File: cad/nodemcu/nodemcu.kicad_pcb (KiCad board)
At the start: 2 copper layers, 1 part, among them P1 CONN_02X15

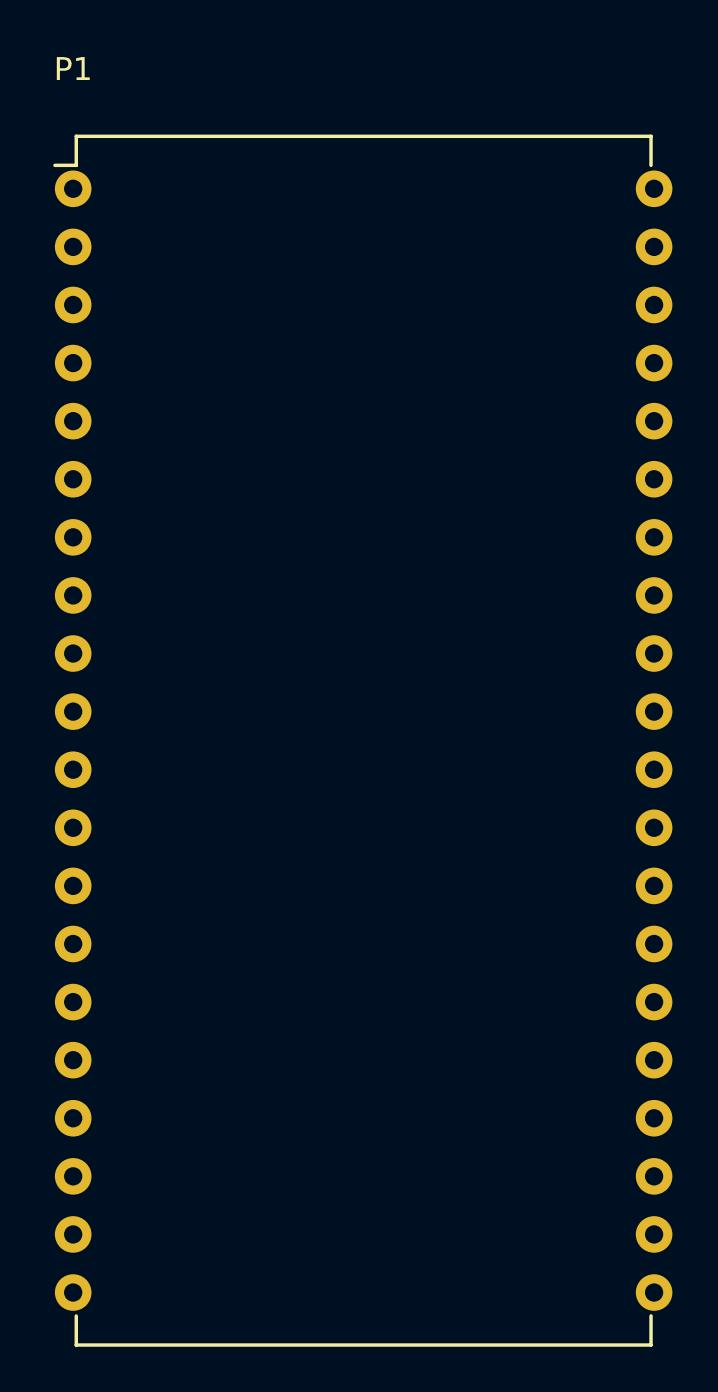
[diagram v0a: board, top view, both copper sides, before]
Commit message: added schematic for nodemcu
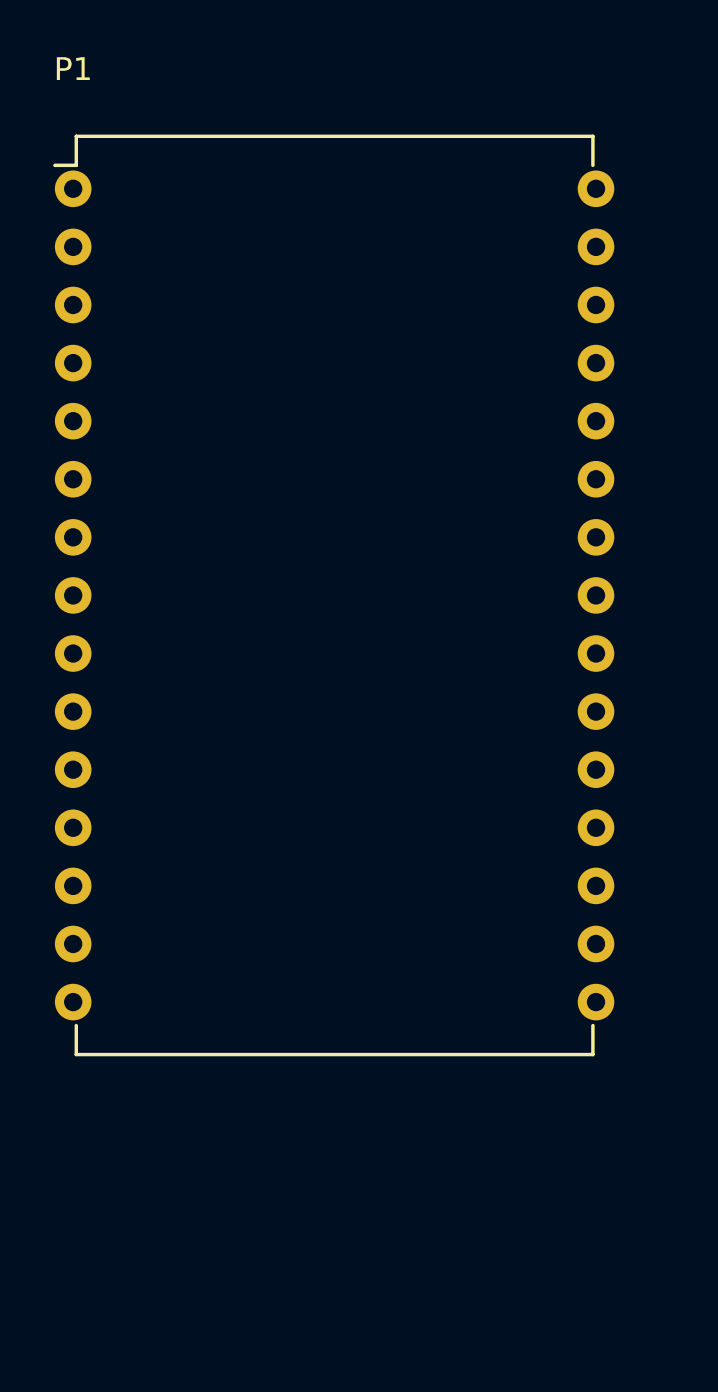
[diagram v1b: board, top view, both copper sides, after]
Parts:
- P1: value CONN_02X15 -> NodeMCU; footprint Housings_DIP:DIP-40_W25.4mm -> nodemcu:NodeMCU
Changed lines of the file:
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@@
     (links 0)
     (no_connects 0)
-    (area 143.392767 98.6586 175.176101 155.978601)
+    (area 144.773719 98.6586 172.626101 143.329253)
     (thickness 1.6)
     (drawings 0)
@@
     (add_net "Net-(P1-Pad9)")
   )
-  (module Housings_DIP:DIP-40_W25.4mm (layer F.Cu)
+  (module nodemcu:NodeMCU (layer F.Cu)
     (at 148.5011 105.0036)
-    (descr "40-lead dip package, row spacing 25.4 mm (1000 mils)")
-    (tags "dil dip 2.54 1000")
+    (descr "64-lead dip package, row spacing 22.86 mm (900 mils)")
+    (tags "dil dip 2.54 900")
     (fp_text reference P1 (at 0 -5.22) (layer F.SilkS)
       (effects (font (size 1 1) (thickness 0.15)))
     )
-    (fp_text value CONN_02X15 (at 0 -3.72) (layer F.Fab)
+    (fp_text value NodeMCU (at 0 -3.72) (layer F.Fab)
       (effects (font (size 1 1) (thickness 0.15)))
     )
-    (fp_line (start -1.05 -2.45) (end -1.05 50.75) (layer F.CrtYd) (width 0.05))
-    (fp_line (start 26.45 -2.45) (end 26.45 50.75) (layer F.CrtYd) (width 0.05))
-    (fp_line (start -1.05 -2.45) (end 26.45 -2.45) (layer F.CrtYd) (width 0.05))
-    (fp_line (start -1.05 50.75) (end 26.45 50.75) (layer F.CrtYd) (width 0.05))
+    (fp_line (start -1.05 -2.45) (end -1.05 38.100596) (layer F.CrtYd) (width 0.05))
+    (fp_line (start 23.9 -2.45) (end 23.9 38.100652) (layer F.CrtYd) (width 0.05))
+    (fp_line (start -1.05 -2.45) (end 23.9 -2.45) (layer F.CrtYd) (width 0.05))
+    (fp_line (start -1.05 38.02) (end 23.9 38.02) (layer F.CrtYd) (width 0.05))
     (fp_line (start 0.135 -2.295) (end 0.135 -1.025) (layer F.SilkS) (width 0.15))
-    (fp_line (start 25.265 -2.295) (end 25.265 -1.025) (layer F.SilkS) (width 0.15))
-    (fp_line (start 25.265 50.555) (end 25.265 49.285) (layer F.SilkS) (width 0.15))
-    (fp_line (start 0.135 50.555) (end 0.135 49.285) (layer F.SilkS) (width 0.15))
-    (fp_line (start 0.135 -2.295) (end 25.265 -2.295) (layer F.SilkS) (width 0.15))
-    (fp_line (start 0.135 50.555) (end 25.265 50.555) (layer F.SilkS) (width 0.15))
+    (fp_line (start 22.725 -2.295) (end 22.725 -1.025) (layer F.SilkS) (width 0.15))
+    (fp_line (start 22.725 37.855) (end 22.725 36.585) (layer F.SilkS) (width 0.15))
+    (fp_line (start 0.135 37.855) (end 0.135 36.585) (layer F.SilkS) (width 0.15))
+    (fp_line (start 0.135 -2.295) (end 22.725 -2.295) (layer F.SilkS) (width 0.15))
+    (fp_line (start 0.135 37.855) (end 22.725 37.855) (layer F.SilkS) (width 0.15))
     (fp_line (start 0.135 -1.025) (end -0.8 -1.025) (layer F.SilkS) (width 0.15))
     (pad 1 thru_hole oval (at 0 0) (size 1.6 1.6) (drill 0.8) (layers *.Cu *.Mask F.SilkS)
@@
     (pad 15 thru_hole oval (at 0 35.56) (size 1.6 1.6) (drill 0.8) (layers *.Cu *.Mask F.SilkS)
       (net 15 "Net-(P1-Pad15)"))
-    (pad 16 thru_hole oval (at 0 38.1) (size 1.6 1.6) (drill 0.8) (layers *.Cu *.Mask F.SilkS)
+    (pad 16 thru_hole oval (at 22.86 35.56) (size 1.6 1.6) (drill 0.8) (layers *.Cu *.Mask F.SilkS)
       (net 16 "Net-(P1-Pad16)"))
-    (pad 17 thru_hole oval (at 0 40.64) (size 1.6 1.6) (drill 0.8) (layers *.Cu *.Mask F.SilkS)
+    (pad 17 thru_hole oval (at 22.86 33.02) (size 1.6 1.6) (drill 0.8) (layers *.Cu *.Mask F.SilkS)
       (net 17 "Net-(P1-Pad17)"))
-    (pad 18 thru_hole oval (at 0 43.18) (size 1.6 1.6) (drill 0.8) (layers *.Cu *.Mask F.SilkS)
+    (pad 18 thru_hole oval (at 22.86 30.48) (size 1.6 1.6) (drill 0.8) (layers *.Cu *.Mask F.SilkS)
       (net 18 "Net-(P1-Pad18)"))
-    (pad 19 thru_hole oval (at 0 45.72) (size 1.6 1.6) (drill 0.8) (layers *.Cu *.Mask F.SilkS)
+    (pad 19 thru_hole oval (at 22.86 27.94) (size 1.6 1.6) (drill 0.8) (layers *.Cu *.Mask F.SilkS)
       (net 19 "Net-(P1-Pad19)"))
-    (pad 20 thru_hole oval (at 0 48.26) (size 1.6 1.6) (drill 0.8) (layers *.Cu *.Mask F.SilkS)
+    (pad 20 thru_hole oval (at 22.86 25.4) (size 1.6 1.6) (drill 0.8) (layers *.Cu *.Mask F.SilkS)
       (net 20 "Net-(P1-Pad20)"))
-    (pad 21 thru_hole oval (at 25.4 48.26) (size 1.6 1.6) (drill 0.8) (layers *.Cu *.Mask F.SilkS)
+    (pad 21 thru_hole oval (at 22.86 22.86) (size 1.6 1.6) (drill 0.8) (layers *.Cu *.Mask F.SilkS)
       (net 21 "Net-(P1-Pad21)"))
-    (pad 22 thru_hole oval (at 25.4 45.72) (size 1.6 1.6) (drill 0.8) (layers *.Cu *.Mask F.SilkS)
+    (pad 22 thru_hole oval (at 22.86 20.32) (size 1.6 1.6) (drill 0.8) (layers *.Cu *.Mask F.SilkS)
       (net 22 "Net-(P1-Pad22)"))
-    (pad 23 thru_hole oval (at 25.4 43.18) (size 1.6 1.6) (drill 0.8) (layers *.Cu *.Mask F.SilkS)
+    (pad 23 thru_hole oval (at 22.86 17.78) (size 1.6 1.6) (drill 0.8) (layers *.Cu *.Mask F.SilkS)
       (net 23 "Net-(P1-Pad23)"))
-    (pad 24 thru_hole oval (at 25.4 40.64) (size 1.6 1.6) (drill 0.8) (layers *.Cu *.Mask F.SilkS)
+    (pad 24 thru_hole oval (at 22.86 15.24) (size 1.6 1.6) (drill 0.8) (layers *.Cu *.Mask F.SilkS)
       (net 24 "Net-(P1-Pad24)"))
-    (pad 25 thru_hole oval (at 25.4 38.1) (size 1.6 1.6) (drill 0.8) (layers *.Cu *.Mask F.SilkS)
+    (pad 25 thru_hole oval (at 22.86 12.7) (size 1.6 1.6) (drill 0.8) (layers *.Cu *.Mask F.SilkS)
       (net 25 "Net-(P1-Pad25)"))
-    (pad 26 thru_hole oval (at 25.4 35.56) (size 1.6 1.6) (drill 0.8) (layers *.Cu *.Mask F.SilkS)
+    (pad 26 thru_hole oval (at 22.86 10.16) (size 1.6 1.6) (drill 0.8) (layers *.Cu *.Mask F.SilkS)
       (net 26 "Net-(P1-Pad26)"))
-    (pad 27 thru_hole oval (at 25.4 33.02) (size 1.6 1.6) (drill 0.8) (layers *.Cu *.Mask F.SilkS)
+    (pad 27 thru_hole oval (at 22.86 7.62) (size 1.6 1.6) (drill 0.8) (layers *.Cu *.Mask F.SilkS)
       (net 27 "Net-(P1-Pad27)"))
-    (pad 28 thru_hole oval (at 25.4 30.48) (size 1.6 1.6) (drill 0.8) (layers *.Cu *.Mask F.SilkS)
+    (pad 28 thru_hole oval (at 22.86 5.08) (size 1.6 1.6) (drill 0.8) (layers *.Cu *.Mask F.SilkS)
       (net 28 "Net-(P1-Pad28)"))
-    (pad 29 thru_hole oval (at 25.4 27.94) (size 1.6 1.6) (drill 0.8) (layers *.Cu *.Mask F.SilkS)
+    (pad 29 thru_hole oval (at 22.86 2.54) (size 1.6 1.6) (drill 0.8) (layers *.Cu *.Mask F.SilkS)
       (net 29 "Net-(P1-Pad29)"))
-    (pad 30 thru_hole oval (at 25.4 25.4) (size 1.6 1.6) (drill 0.8) (layers *.Cu *.Mask F.SilkS)
+    (pad 30 thru_hole oval (at 22.86 0) (size 1.6 1.6) (drill 0.8) (layers *.Cu *.Mask F.SilkS)
       (net 30 "Net-(P1-Pad30)"))
-    (pad 31 thru_hole oval (at 25.4 22.86) (size 1.6 1.6) (drill 0.8) (layers *.Cu *.Mask F.SilkS))
-    (pad 32 thru_hole oval (at 25.4 20.32) (size 1.6 1.6) (drill 0.8) (layers *.Cu *.Mask F.SilkS))
-    (pad 33 thru_hole oval (at 25.4 17.78) (size 1.6 1.6) (drill 0.8) (layers *.Cu *.Mask F.SilkS))
-    (pad 34 thru_hole oval (at 25.4 15.24) (size 1.6 1.6) (drill 0.8) (layers *.Cu *.Mask F.SilkS))
-    (pad 35 thru_hole oval (at 25.4 12.7) (size 1.6 1.6) (drill 0.8) (layers *.Cu *.Mask F.SilkS))
-    (pad 36 thru_hole oval (at 25.4 10.16) (size 1.6 1.6) (drill 0.8) (layers *.Cu *.Mask F.SilkS))
-    (pad 37 thru_hole oval (at 25.4 7.62) (size 1.6 1.6) (drill 0.8) (layers *.Cu *.Mask F.SilkS))
-    (pad 38 thru_hole oval (at 25.4 5.08) (size 1.6 1.6) (drill 0.8) (layers *.Cu *.Mask F.SilkS))
-    (pad 39 thru_hole oval (at 25.4 2.54) (size 1.6 1.6) (drill 0.8) (layers *.Cu *.Mask F.SilkS))
-    (pad 40 thru_hole oval (at 25.4 0) (size 1.6 1.6) (drill 0.8) (layers *.Cu *.Mask F.SilkS))
-    (model Housings_DIP.3dshapes/DIP-40_W25.4mm.wrl
-      (at (xyz 0 0 0))
-      (scale (xyz 1 1 1))
-      (rotate (xyz 0 0 0))
+    (model /home/thomas/workspace/LaundryMeasure/cad/nodemcu/nodemcu.x3d
+      (at (xyz -0.09 -1.65 0.15))
+      (scale (xyz 0.4 0.4 0.4))
+      (rotate (xyz -90 0 180))
     )
   )
